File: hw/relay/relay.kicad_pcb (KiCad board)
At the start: 2 copper layers, 32.7 x 40.3 mm, 14 parts, among them J1 trigger input, J2 power input, J3 output terminal, K1 G5LE-1, Q1 PN2222A

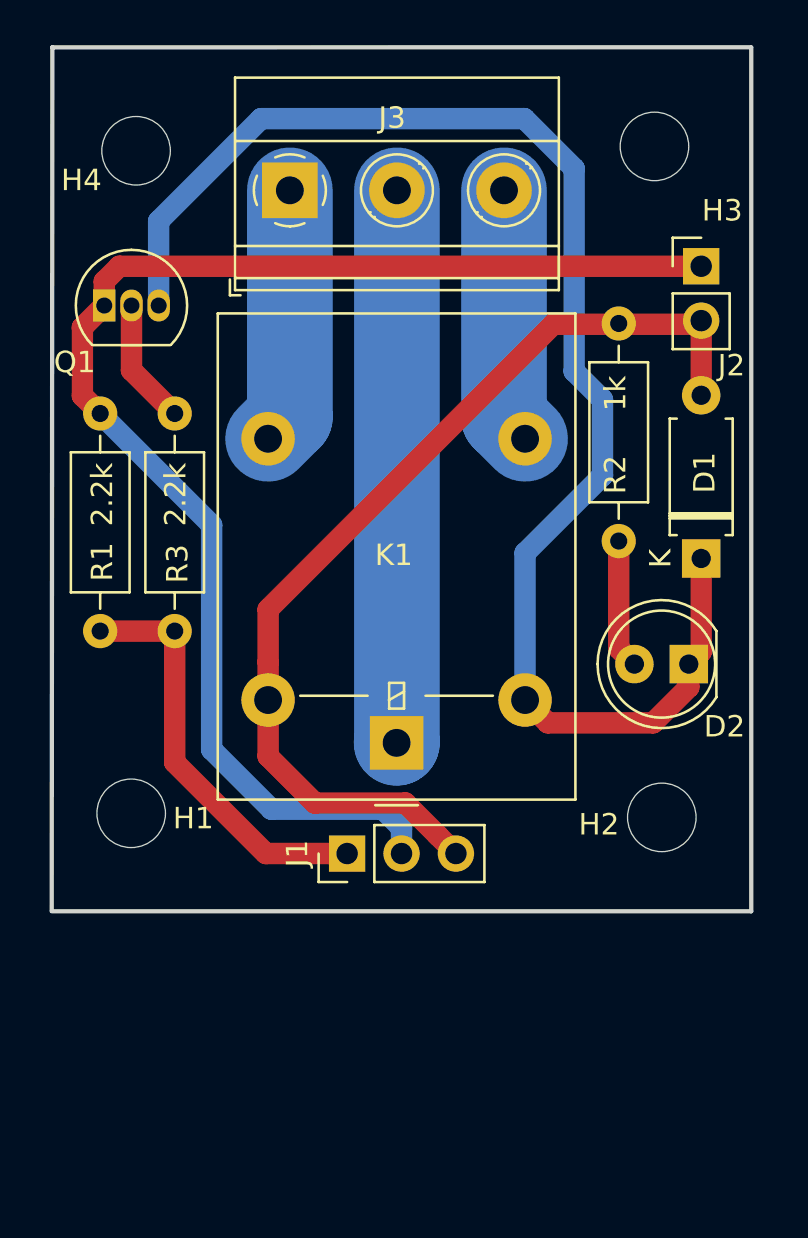
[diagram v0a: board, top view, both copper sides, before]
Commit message: RELAY bus connection
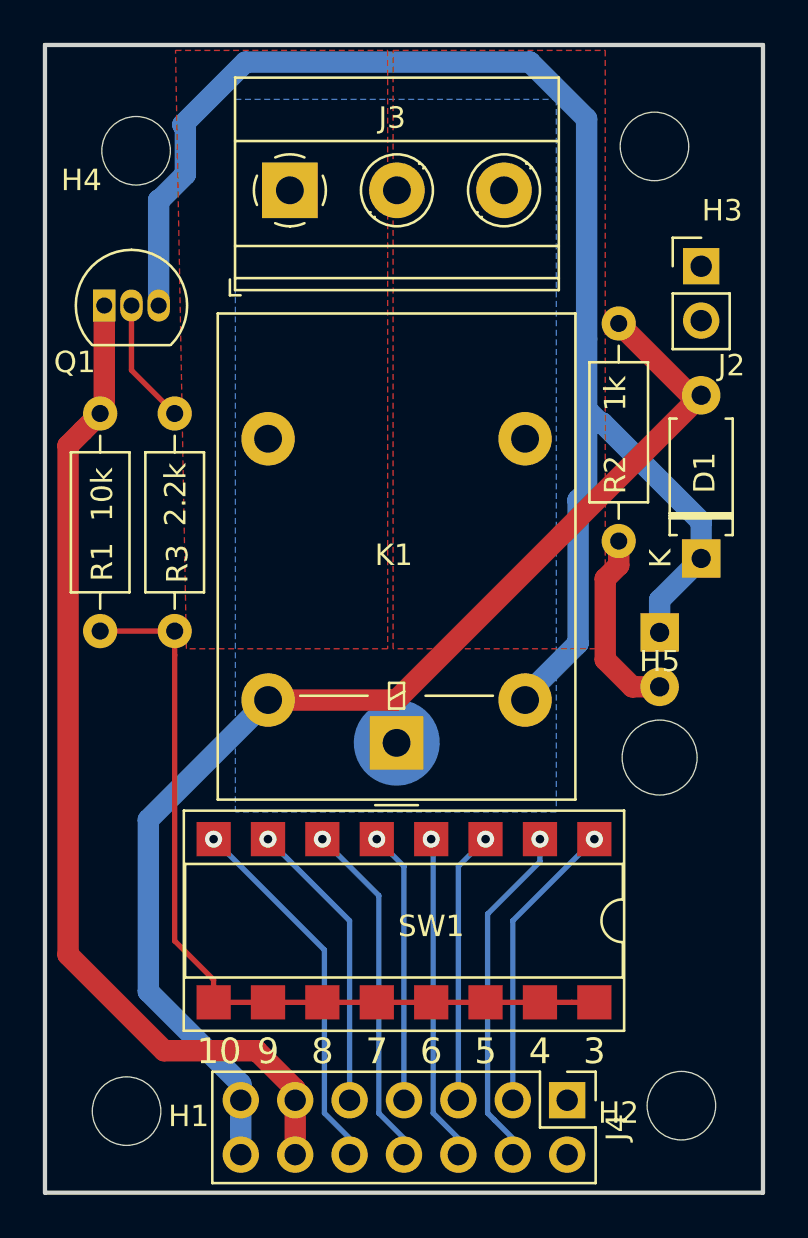
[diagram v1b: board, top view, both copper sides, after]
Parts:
- removed J1: trigger input, Connector_PinHeader_2.54mm:PinHeader_1x03_P2.54mm_Vertical
- added H5: MountingHole_Pad, MountingHole:MountingHole_3.5mm, F.Cu at (112.3, 91.2)
- added J4: BUS, Connector_PinHeader_2.54mm:PinHeader_2x07_P2.54mm_Vertical, F.Cu at (108.0, 107.2)
- added SW1: SW_DIP_x08, Package_DIP:DIP-16_W7.62mm_SMDSocket_SmallPads, F.Cu at (100.3, 98.8)
- D2: moved to B.Cu
- R1: value 2.2k -> 10k
- moved H1 13.9 mm to (87.4, 107.7)
- moved H2 13.5 mm to (113.3, 107.4)
- moved D2 2.01 mm to (112.3, 85.3), turned to 270 degrees
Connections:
- D1 pad 2: VCC -> bus13
- K1 pad 5: VCC -> bus13
- Q1 pad 1: GND -> bus11
- R1 pad 1: GND -> bus11
- R2 pad 1: VCC -> bus13
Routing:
- net GND: track 64.5 -> 0.00 mm
- net bus13: track 0.00 -> 55.9 mm
- net VCC: track 46.8 -> 0.24 mm
- net bus11: track 0.00 -> 46.5 mm
- net relay_arm: track 25.8 -> 0.02 mm
- net trigger: track 19.4 -> 39.3 mm
- net bus10: track 0.00 -> 16.6 mm, vias 0 -> 1
- net bus8: track 0.00 -> 15.5 mm, vias 0 -> 1
- net bus4: track 0.00 -> 15.5 mm, vias 0 -> 1
- net bus6: track 0.00 -> 14.5 mm, vias 0 -> 1
- net bus9: track 0.00 -> 13.0 mm, vias 0 -> 1
- net bus3: track 0.00 -> 13.0 mm, vias 0 -> 1
- net relay_off: track 12.0 -> 0.00 mm
- net relay_on: track 12.0 -> 0.00 mm
- net bus7: track 0.00 -> 12.0 mm, vias 0 -> 1
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- added copper zone on B.Cu, net relay_arm
- added copper zone on F.Cu, net relay_off
- added copper zone on F.Cu, net relay_on
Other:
- board size 32.7 x 40.3 mm -> 33.5 x 53.6 mm
- board text added: "10"
- board text added: "3"
- board text added: "4"
- board text added: "5"
- board text added: "6"
- board text added: "7"
- board text added: "8"
- board text added: "9"

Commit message: relay layout changes
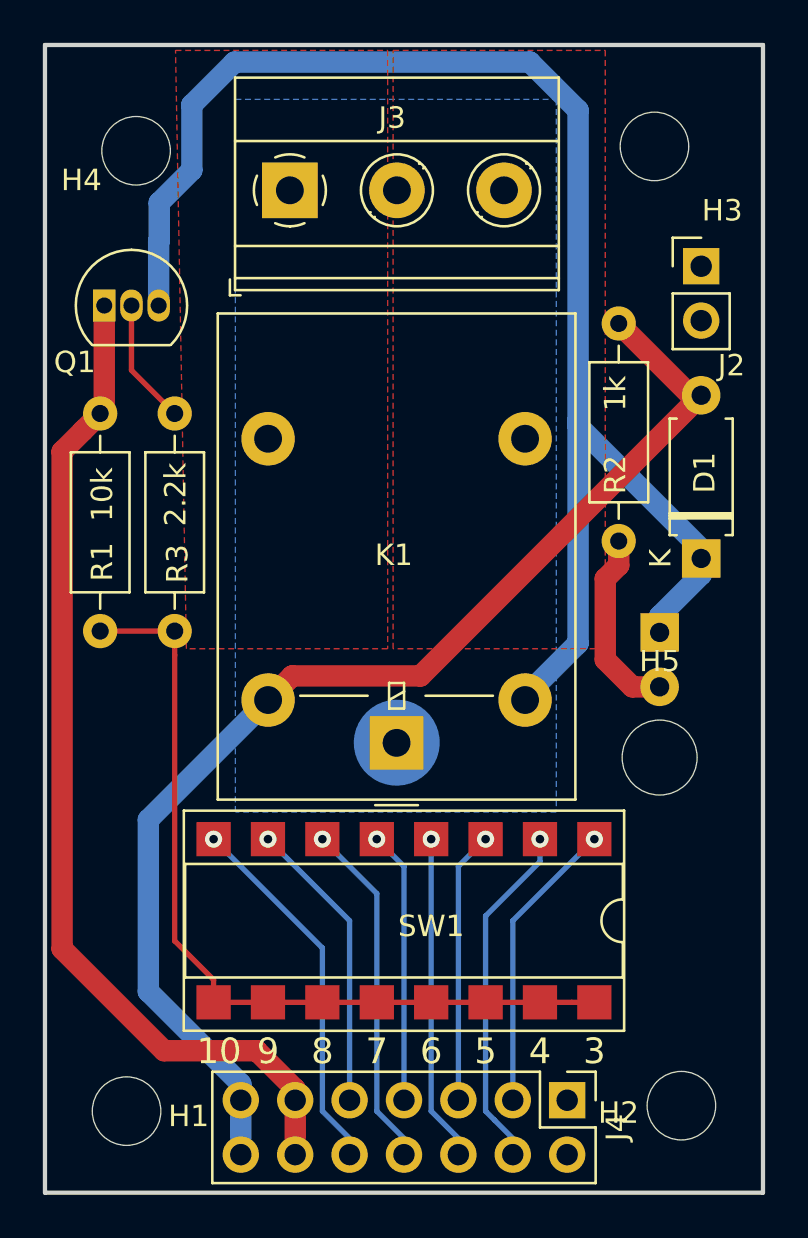
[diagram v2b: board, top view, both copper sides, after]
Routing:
- net Net-(D1-Pad1): track 72.0 -> 71.5 mm
